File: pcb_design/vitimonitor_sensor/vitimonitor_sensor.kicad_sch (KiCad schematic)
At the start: 26 parts, among them J1 USB_C_Receptacle_USB2.0_14P, SW1 BOOT, SW2 RESETN, U1 ESP32-C3-WROOM-02U, U2 USBLC6-2SC6, U3 LM1117DT-3.3

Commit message: Kicad Schematic Update
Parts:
- added D5: ESD3V3, Diode_SMD:D_SOD-923, symbol Diode:ESD9B3.3ST5G
- added J2: Conn_01x10, symbol Connector_Generic:Conn_01x10
- added J3: Conn_01x02, symbol Connector_Generic:Conn_01x02
- added J4: Conn_01x04, symbol Connector_Generic:Conn_01x04
- added R8, R9: 2.2k, symbol Device:R_Small
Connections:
- net +3.3V: now also J2.10 (Pin_10), J4.1 (Pin_1), R8.1, R9.1
- net +5V: now also J2.1 (Pin_1)
- net BOOT: now also J2.8 (Pin_8)
- net EN: now also J2.9 (Pin_9)
- net GND: now also D5.1 (A1), J2.2 (Pin_2), J3.1 (Pin_1), J4.4 (Pin_4)
- net GPIO2: now also J2.6 (Pin_6)
- net GPIO8: now also J2.7 (Pin_7)
- net USB_D+: now also U1.14 (IO19), J2.3 (Pin_3); no longer U1.13 (IO18)
- net USB_D-: now also U1.13 (IO18), J2.4 (Pin_4); no longer U1.14 (IO19)
- net at F1.2, FB1.1: now also D5.2 (A2)
- net GPIO3: now reaches U1.15 (IO3)
- net GPIO1: now reaches U1.17 (IO1)
- net GPIO0: now reaches U1.18 (IO0)
- net GPIO0: now also J2.5 (Pin_5)
- net GPIO4: now reaches U1.3 (IO4)
- new net SCL: J4.2 (Pin_2), R8.2
- new net SDA: J4.3 (Pin_3), R9.2
- new net VBAT: J3.2 (Pin_2)
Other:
- note added: "BATTERY CONNECTOR"
- note added: "I2C CONNETOR"
- note added: "MAIN SIGNALS CONNETOR"
- moved on the sheet: C1, C5, C6, D1, FB1, R6, R7, U1, U2

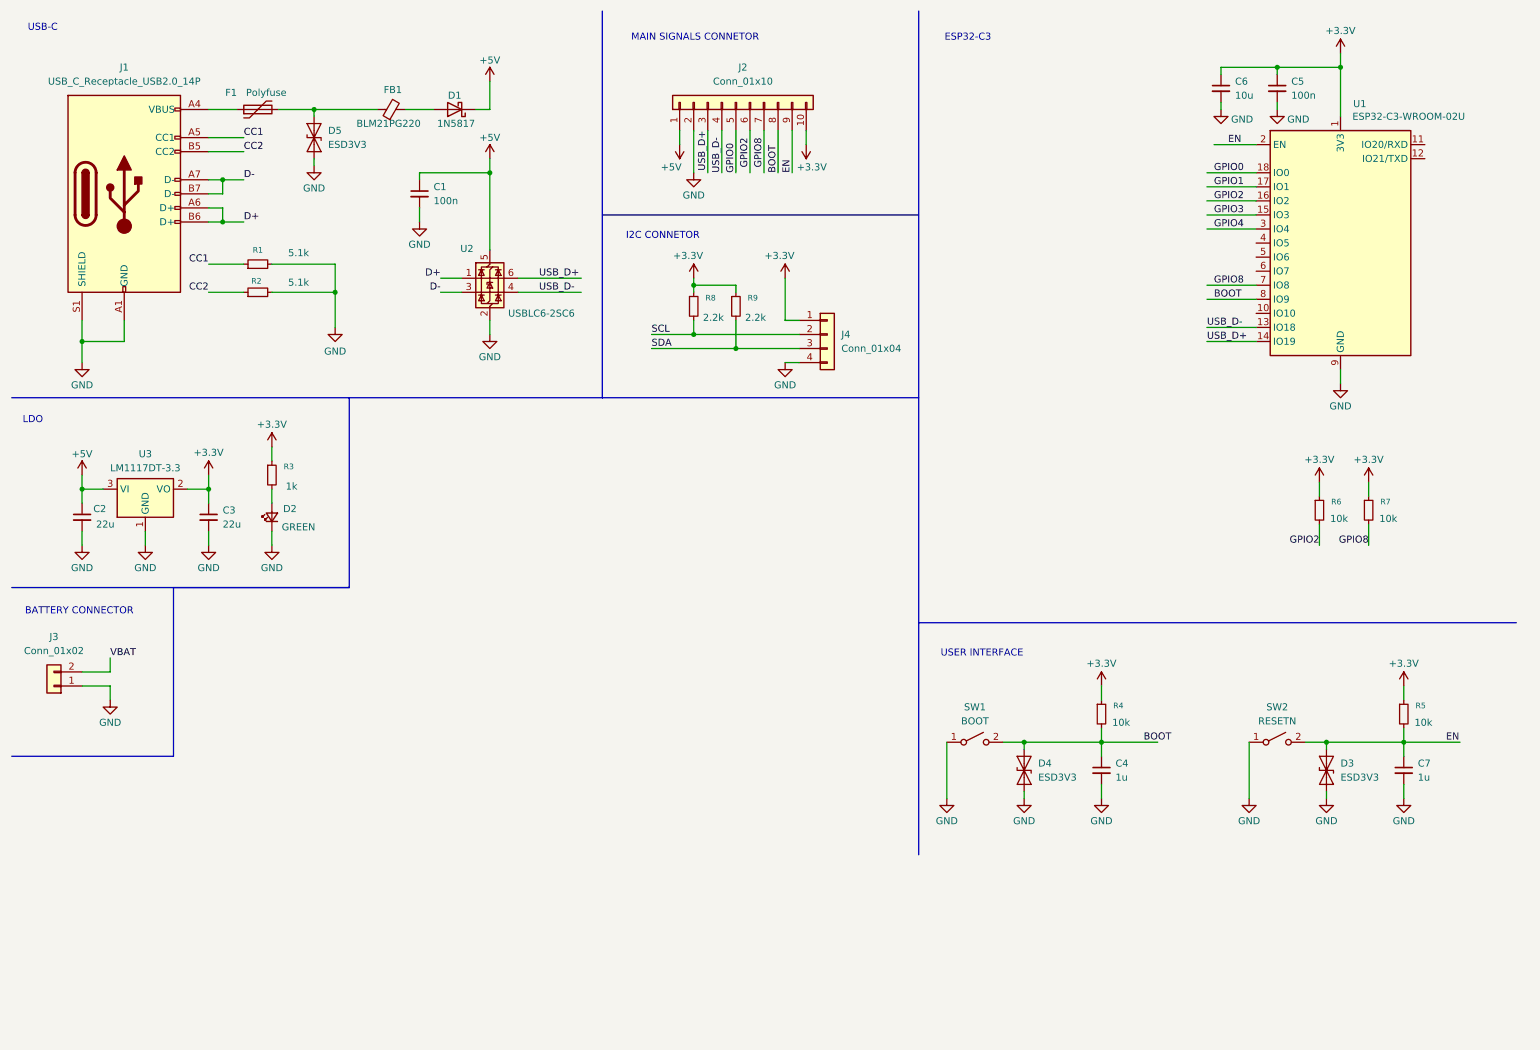
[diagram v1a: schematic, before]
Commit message: Schematic improvements
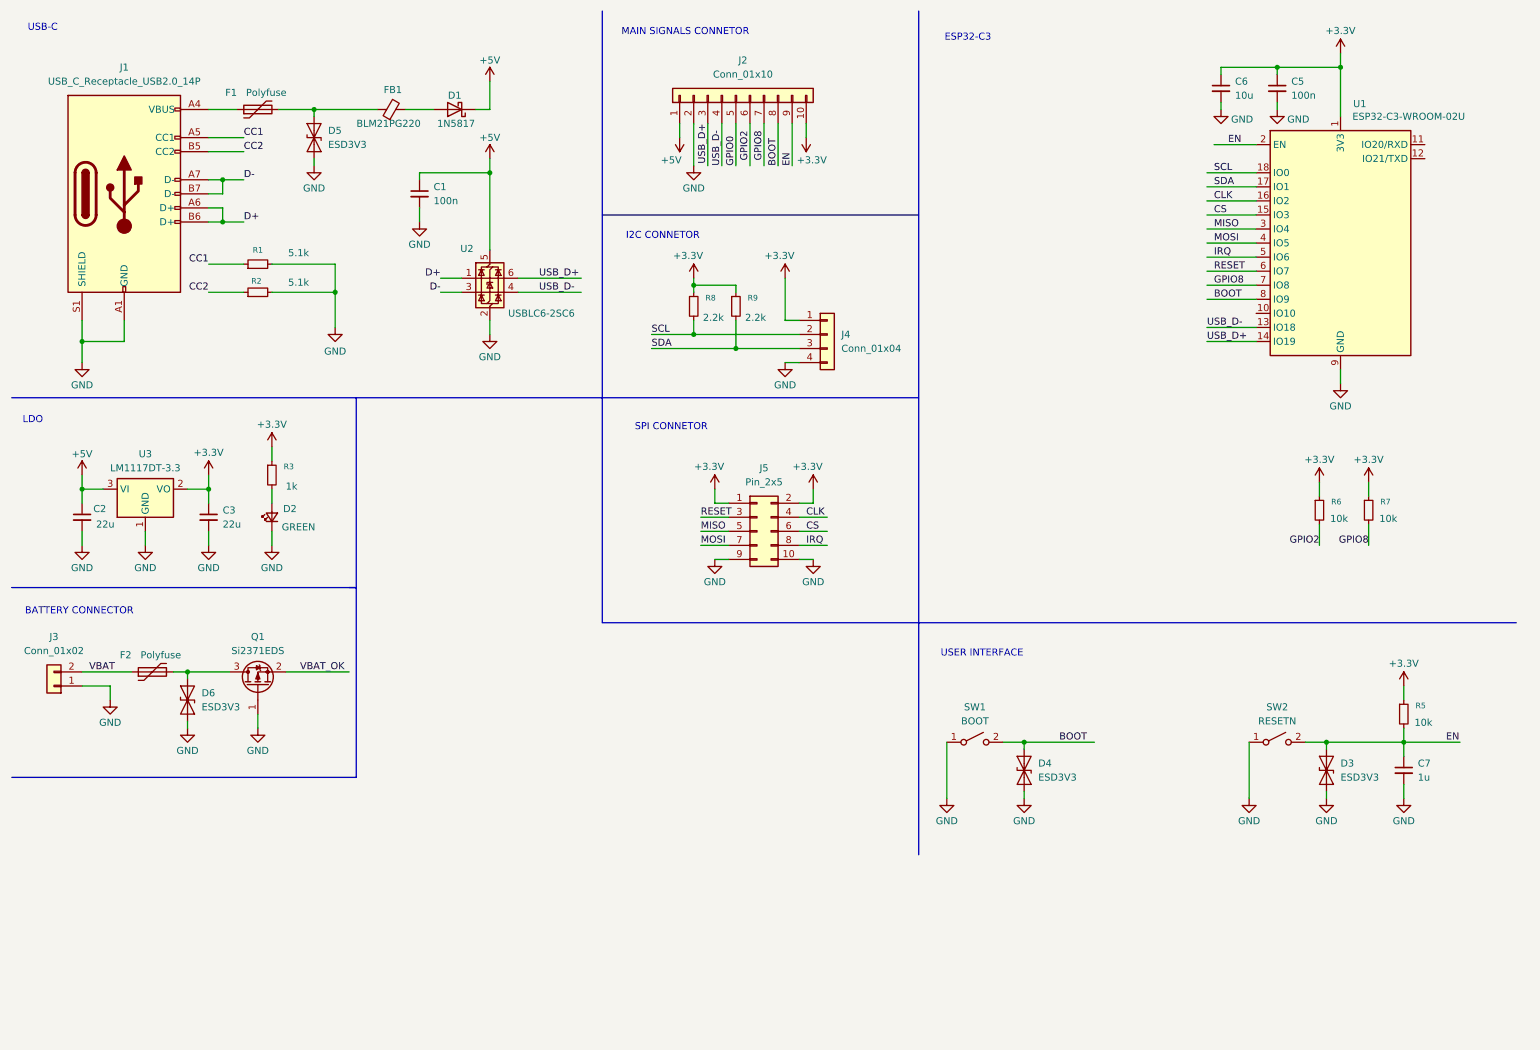
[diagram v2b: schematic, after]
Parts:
- removed C4: 1u, symbol Device:C_Small
- removed R4: 10k, symbol Device:R_Small
- added D6: ESD3V3, Diode_SMD:D_SOD-923, symbol Diode:ESD9B3.3ST5G
- added F2: Polyfuse, symbol Device:Polyfuse
- added J5: Pin_2x5, symbol Connector_Generic:Conn_02x05_Odd_Even
- added Q1: Si2371EDS, Package_TO_SOT_SMD:SOT-23, symbol Transistor_FET:Si2371EDS
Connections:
- net GPIO1 is gone; now on net SDA: U1.17 (IO1)
- net +3.3V: now also J5.1 (Pin_1), J5.2 (Pin_2)
- net GND: now also D6.1 (A1), J5.10 (Pin_10), J5.9 (Pin_9), Q1.1 (G)
- net GPIO0: no longer U1.18 (IO0)
- net GPIO2: no longer U1.16 (IO2)
- net SCL: now also U1.18 (IO0)
- net VBAT: now also F2.1
- net MOSI: now reaches U1.4 (IO5)
- net MOSI: now also J5.7 (Pin_7)
- net IRQ: now reaches U1.5 (IO6)
- net IRQ: now also J5.8 (Pin_8)
- net RESET: now reaches U1.6 (IO7)
- net RESET: now also J5.3 (Pin_3)
- net GPIO3 renamed CS
- net CS: now also J5.6 (Pin_6)
- net GPIO4 renamed MISO
- net MISO: now also J5.5 (Pin_5)
- new net: D6.2 (A2), F2.2, Q1.3 (D)
- new net CLK: J5.4 (Pin_4), U1.16 (IO2)
- new net VBAT_OK: Q1.2 (S)
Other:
- note added: "SPI CONNETOR"
- moved on the sheet: J2

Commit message: Power management with BQ24075 added
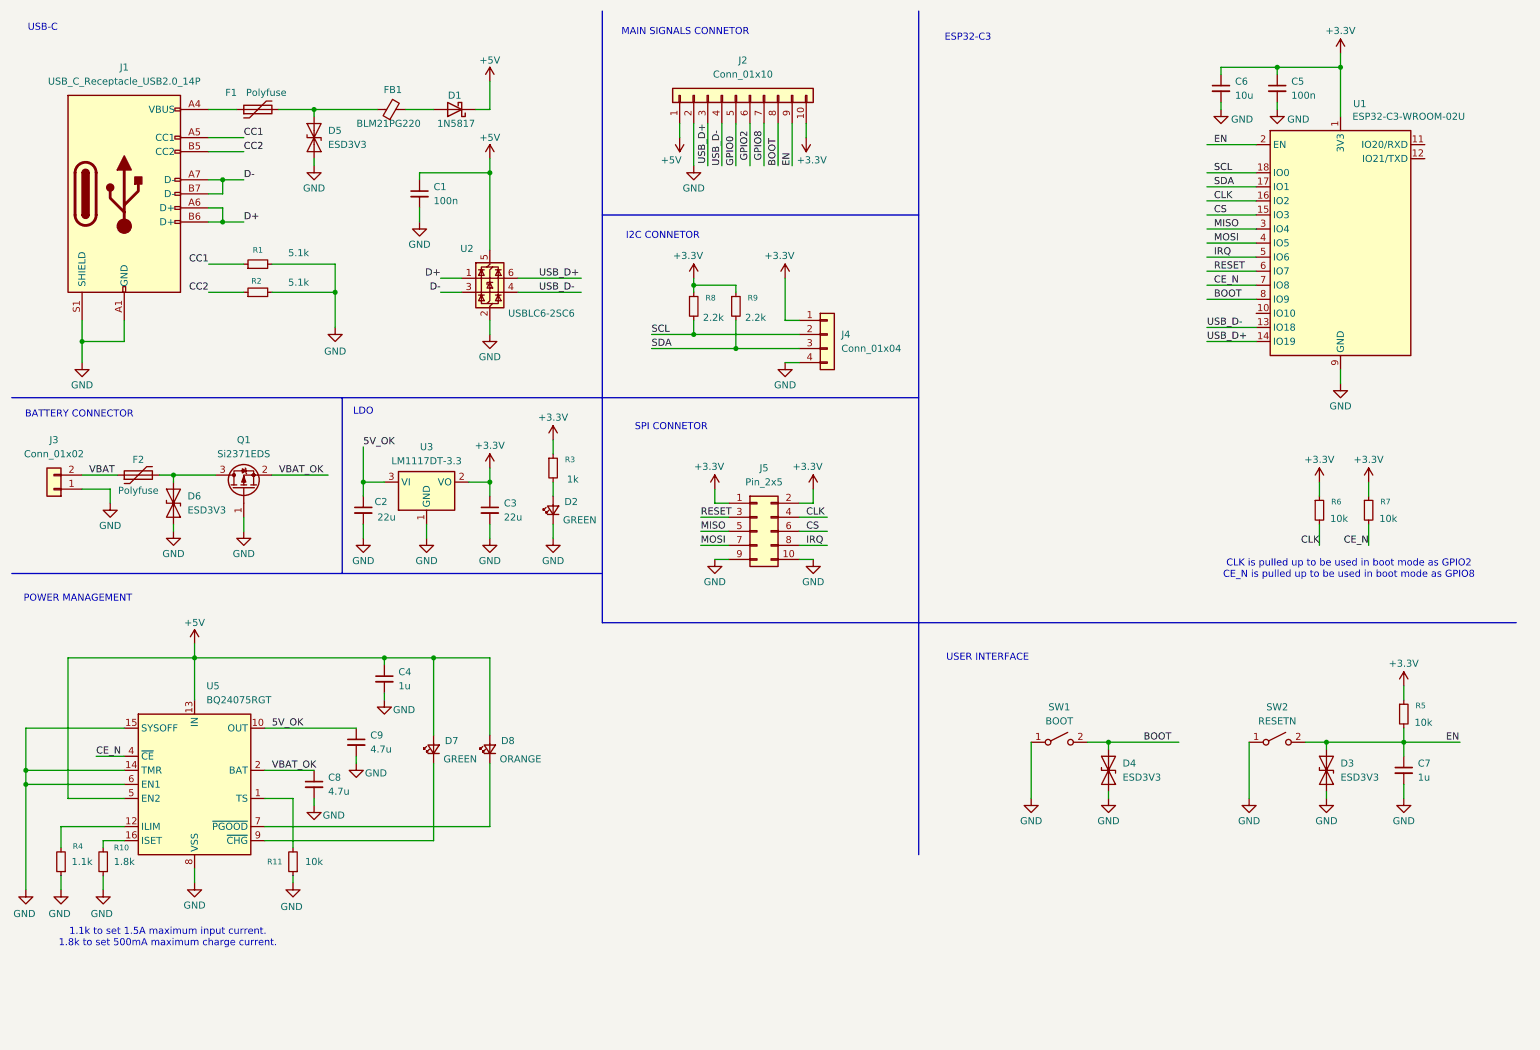
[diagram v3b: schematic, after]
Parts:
- added C4: 1u, symbol Device:C_Small
- added C8, C9: 4.7u, symbol Device:C_Small
- added D7: GREEN, symbol Device:LED_Small
- added D8: ORANGE, symbol Device:LED_Small
- added R10: 1.8k, symbol Device:R_Small
- added R11: 10k, symbol Device:R_Small
- added R4: 1.1k, symbol Device:R_Small
- added U5: BQ24075RGT, Package_DFN_QFN:VQFN-16-1EP_3x3mm_P0.5mm_EP1.6x1.6mm, symbol Battery_Management:BQ24075RGT
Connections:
- net +5V: now also C4.1, D7.2 (A), D8.2 (A), U5.13 (IN), U5.5 (EN2); no longer C2.1, U3.3 (VI)
- net CLK: now also R6.2
- net GND: now also C4.2, C8.2, C9.2, R10.1, R11.1, R4.1, U5.14 (TMR), U5.15 (SYSOFF), U5.17 (VSS), U5.6 (EN1), U5.8 (VSS)
- net GPIO2: no longer R6.2
- net GPIO8: no longer R7.2, U1.7 (IO8)
- net VBAT_OK: now also C8.1, U5.2 (BAT), U5.3 (BAT)
- new net: R11.2, U5.1 (TS)
- new net: R4.2, U5.12 (ILIM)
- new net: R10.2, U5.16 (ISET)
- new net: D8.1 (K), U5.7 (~{PGOOD})
- new net: D7.1 (K), U5.9 (~{CHG})
- new net 5V_OK: C2.1, C9.1, U3.3 (VI), U5.10 (OUT), U5.11 (OUT)
- new net CE_N: R7.2, U1.7 (IO8), U5.4 (~{CE})
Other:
- note added: "1.1k to set 1.5A maximum input current. 1.8k to set 500mA maximum charge current."
- note added: "CLK is pulled up to be used in boot mode as GPIO2 CE_N is pulled up to be used in boot mode as GPIO8"
- note added: "POWER MANAGEMENT"
- moved on the sheet: C2, C3, D2, D4, D6, F2, J3, Q1, R3, SW1, U3

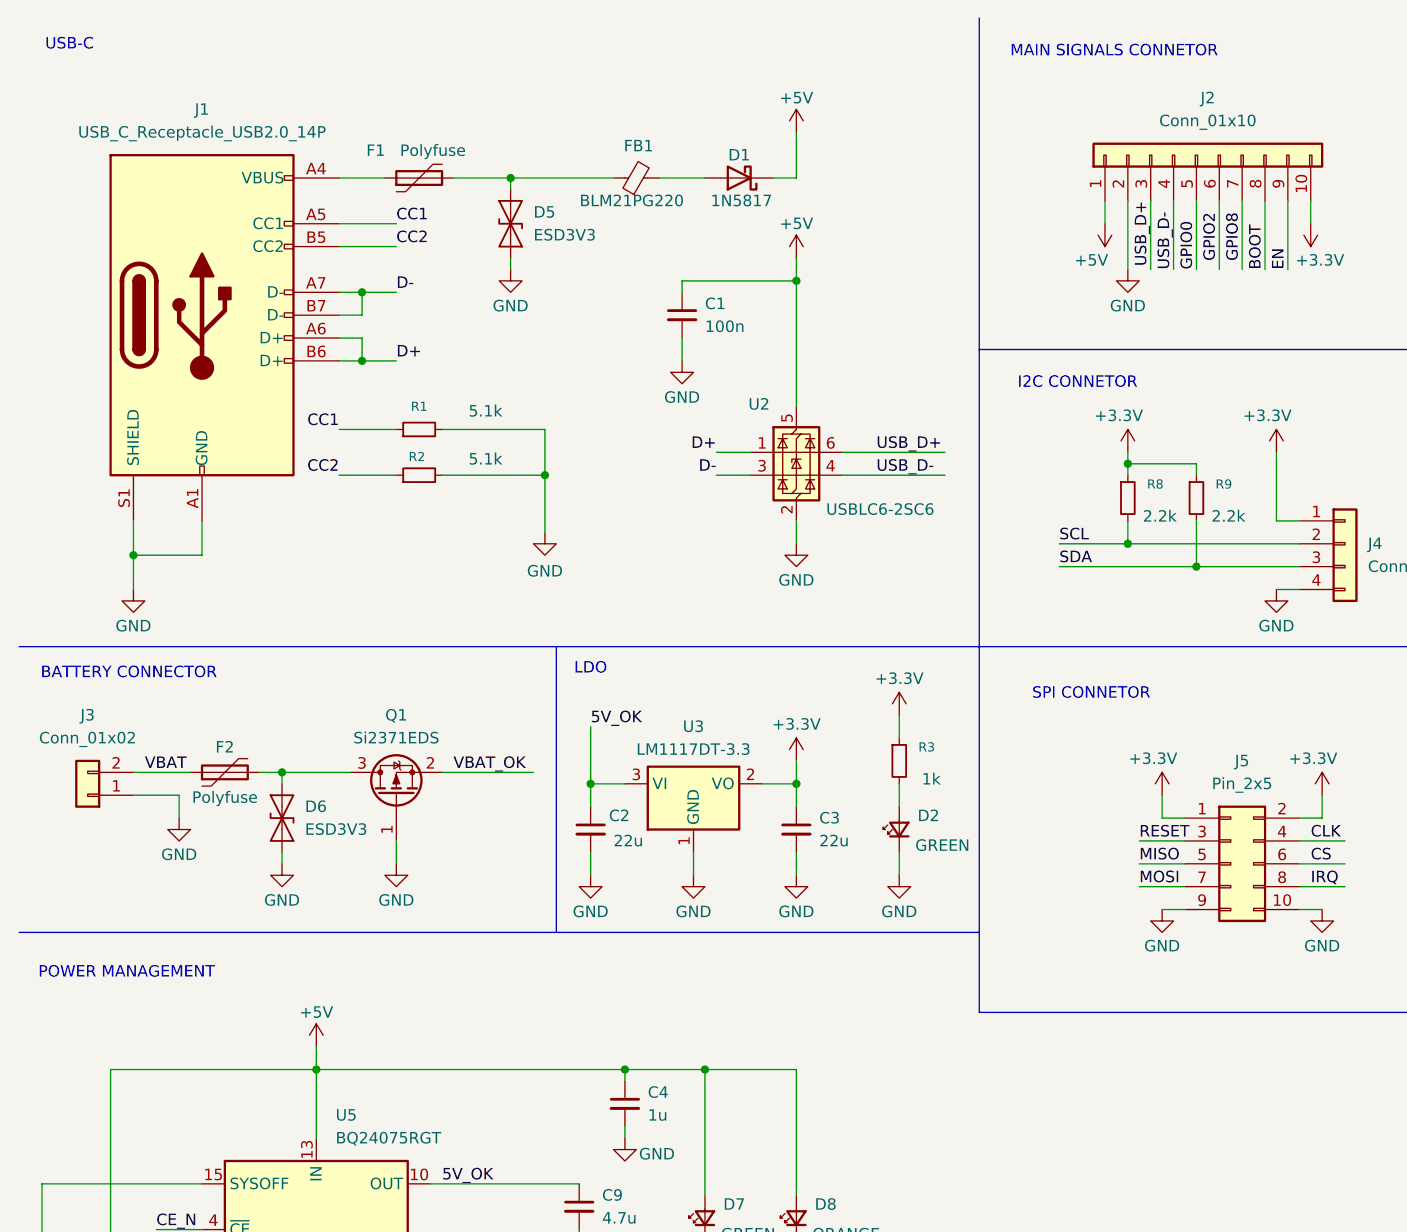
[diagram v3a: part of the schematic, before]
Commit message: Power management with BQ24075 added
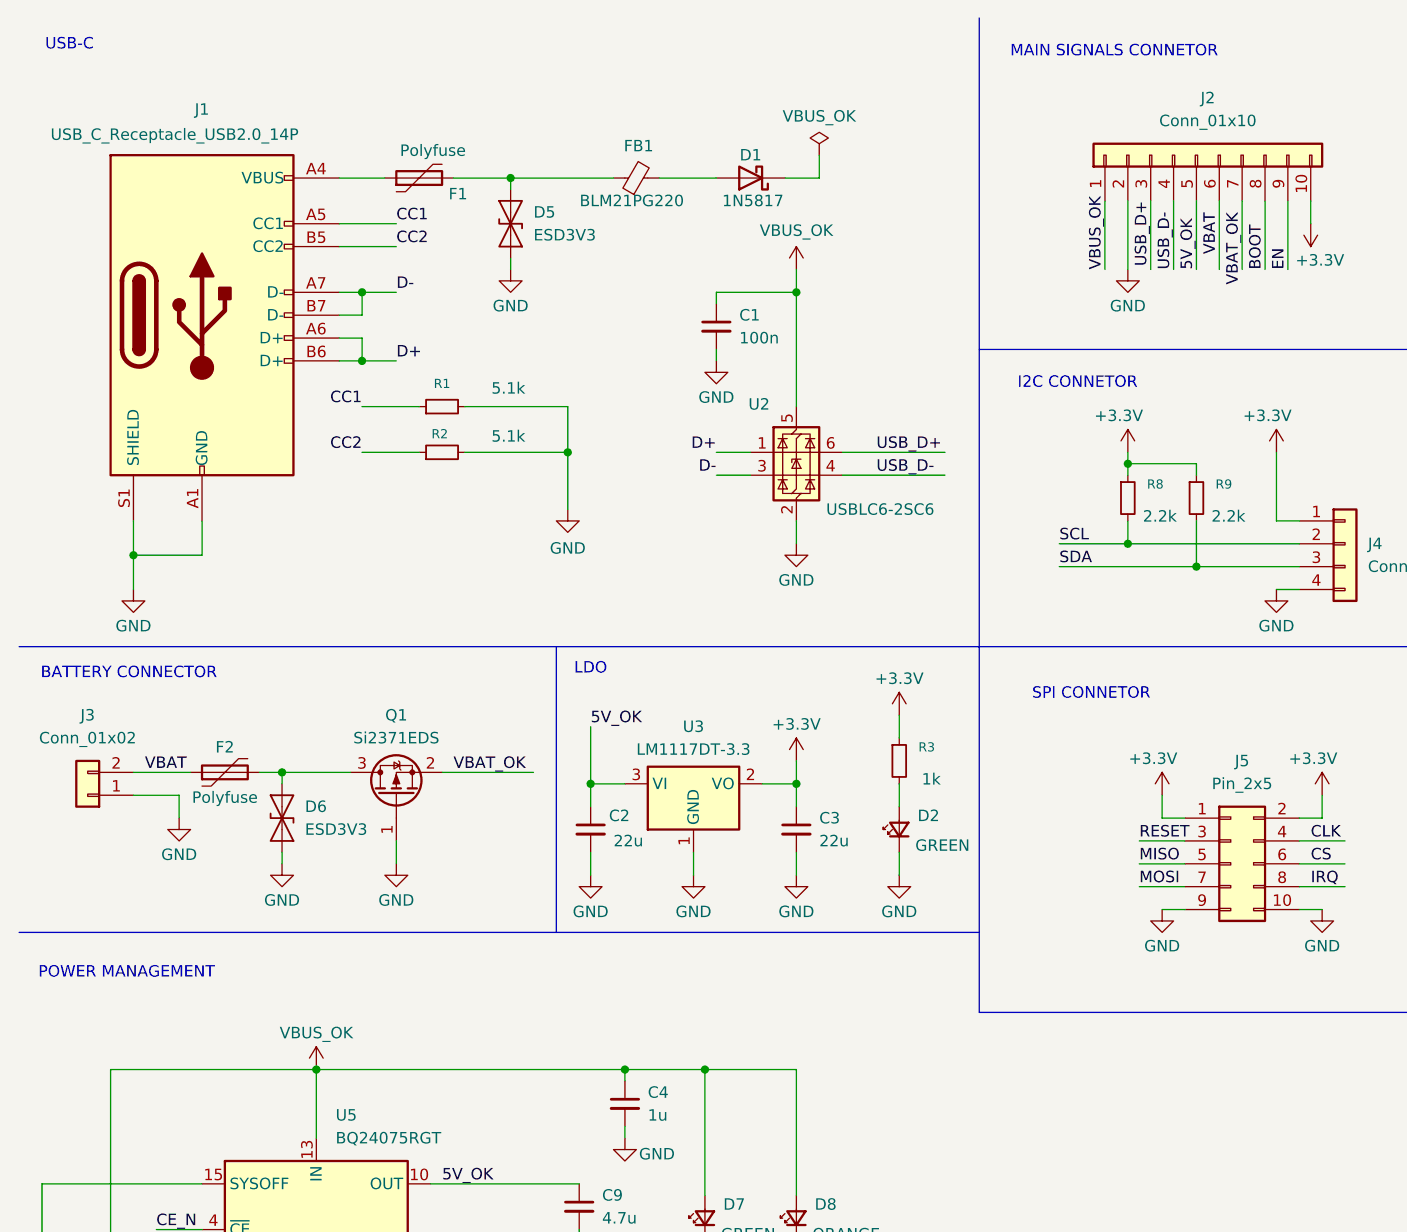
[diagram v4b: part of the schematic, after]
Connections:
- net GPIO0 is gone; now on net 5V_OK: J2.5 (Pin_5)
- net GPIO2 is gone; now on net VBAT: J2.6 (Pin_6)
- net GPIO8 is gone; now on net VBAT_OK: J2.7 (Pin_7)
- net +5V renamed VBUS_OK
- net VBUS_OK: no longer D1.1 (K)
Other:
- moved on the sheet: C1, D1, R1, R2
